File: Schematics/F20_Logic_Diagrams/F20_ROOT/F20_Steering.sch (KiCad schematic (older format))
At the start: 3 parts

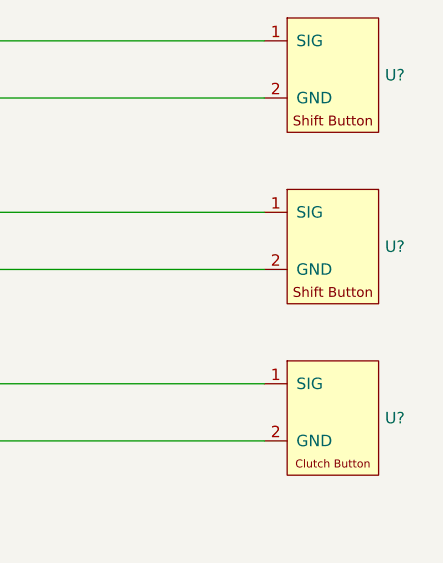
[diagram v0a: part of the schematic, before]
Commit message: Re-annotated Logic Diagrams, pulled a BOM list based on Logic Diagrams
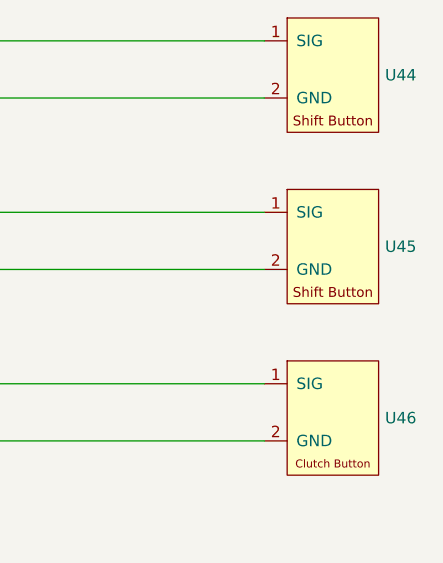
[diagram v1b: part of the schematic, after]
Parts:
- gave numbers to parts that had none: 3
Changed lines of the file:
@@
 $EndDescr
 $Comp
-L FSAE_Library:ShiftButton U?
+L FSAE_Library:ShiftButton U44
 U 1 1 5E684F2E
 P 7000 2500
-F 0 "U?" H 7528 2350 50  0000 L CNN
+F 0 "U44" H 7528 2350 50  0000 L CNN
 F 1 "ShiftButton" H 7350 2650 50  0001 C CNN
 F 2 "" H 7500 3000 50  0001 C CNN
@@
 $EndComp
 $Comp
-L FSAE_Library:ShiftButton U?
+L FSAE_Library:ShiftButton U45
 U 1 1 5E687B8D
 P 7000 3250
-F 0 "U?" H 7528 3100 50  0000 L CNN
+F 0 "U45" H 7528 3100 50  0000 L CNN
 F 1 "ShiftButton" H 7350 3400 50  0001 C CNN
 F 2 "" H 7500 3750 50  0001 C CNN
@@
 $EndComp
 $Comp
-L FSAE_Library:ClutchButton U?
+L FSAE_Library:ClutchButton U46
 U 1 1 5E6898FF
 P 7000 4000
-F 0 "U?" H 7528 3850 50  0000 L CNN
+F 0 "U46" H 7528 3850 50  0000 L CNN
 F 1 "ClutchButton" H 7350 4150 50  0001 C CNN
 F 2 "" H 7500 4500 50  0001 C CNN
@@
 $EndComp
 $Comp
-L FSAE_Library:GND #PWR?
+L FSAE_Library:GND #PWR021
 U 1 1 5E68AA55
 P 5500 4500
-F 0 "#PWR?" H 5500 4300 50  0001 C CNN
+F 0 "#PWR021" H 5500 4300 50  0001 C CNN
 F 1 "GND" H 5504 4346 50  0000 C CNN
 F 2 "" H 5500 4450 50  0001 C CNN
